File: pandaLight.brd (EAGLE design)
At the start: 100 x 50 mm, 161 parts, among them J1 PJ-037A, U1 MIC23450AAAYML, U10 AS4C128M16D3, U11 PMOD-2X6, U12 PMOD-2X6, U13 PLR135-T10, U14 PLT133-T10W, U15 PLR135-T10, U16 TP10SQ, U17 TP10SQ, U18 PAN1322, U2 6SLX45CSG324, U3 TPD4S014SON, U4 FT2232HL, U5 93LC46BT-I/OT, U6 TPD12S016PWR, U7 TPD12S016PWR, U8 N25Q128AF8, U9 TPD12S016PWR, X1 USBUB-S, X2 HDMI_RECEPTICAL_A, X3 HDMI_RECEPTICAL_A, X4 HDMI_RECEPTICAL_A, Y1 403, Y2 20Mhz

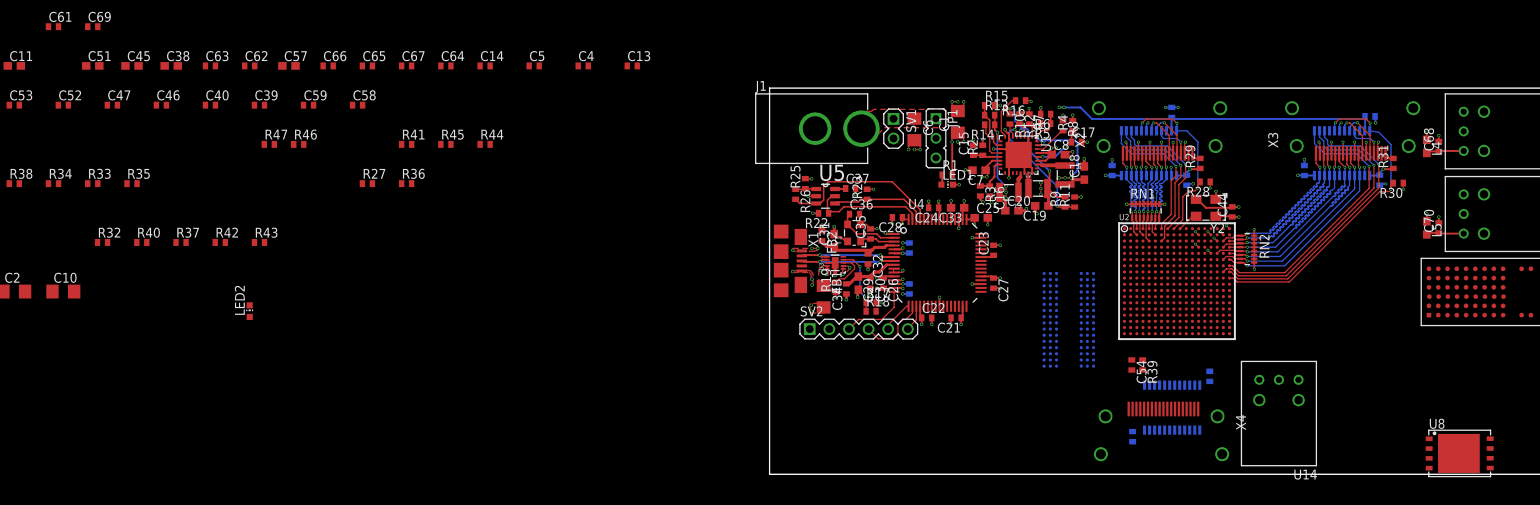
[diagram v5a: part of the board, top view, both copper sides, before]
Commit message: Placed some bypass capacitors
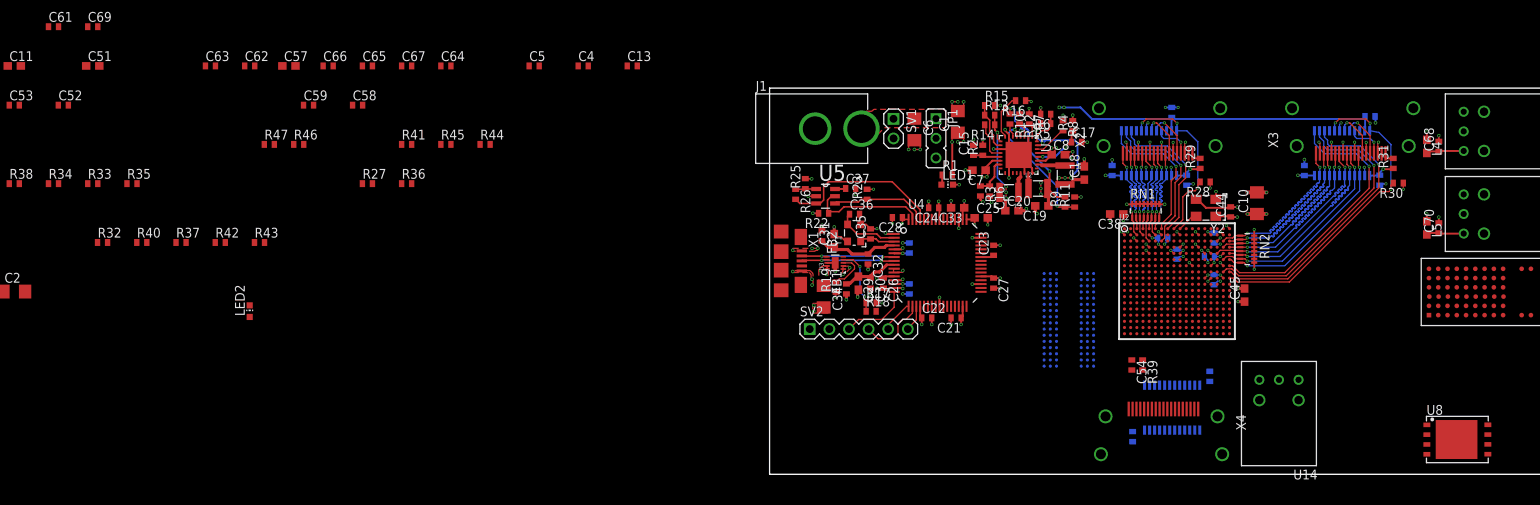
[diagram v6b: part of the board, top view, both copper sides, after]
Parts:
- moved C10 155.0 mm to (63.1, 35.1), turned to 90 degrees
- moved C45 147.1 mm to (61.5, 23.2), turned to 90 degrees
- moved C47 144.4 mm to (57.5, 25.2), flipped to the bottom, turned to 270 degrees
- moved C46 137.1 mm to (57.0, 28.2), flipped to the bottom
- moved C40 131.1 mm to (57.5, 30.6), flipped to the bottom, turned to 270 degrees
- moved C38 123.9 mm to (45.0, 33.7), turned to 180 degrees
- moved C39 118.2 mm to (50.9, 30.6), flipped to the bottom, turned to 180 degrees
- moved C14 92.8 mm to (52.8, 28.5), flipped to the bottom, turned to 270 degrees
- moved U8 1.82 mm to (89.0, 4.50)
- moved C44 0.20 mm to (59.7, 34.0)
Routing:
- net +3V3: track 58.0 -> 77.0 mm, vias 31 -> 47
- net GND: track 104.1 -> 116.9 mm, vias 90 -> 107
- net N$28: track 11.0 -> 10.1 mm
- net N$7: track 13.4 -> 12.8 mm

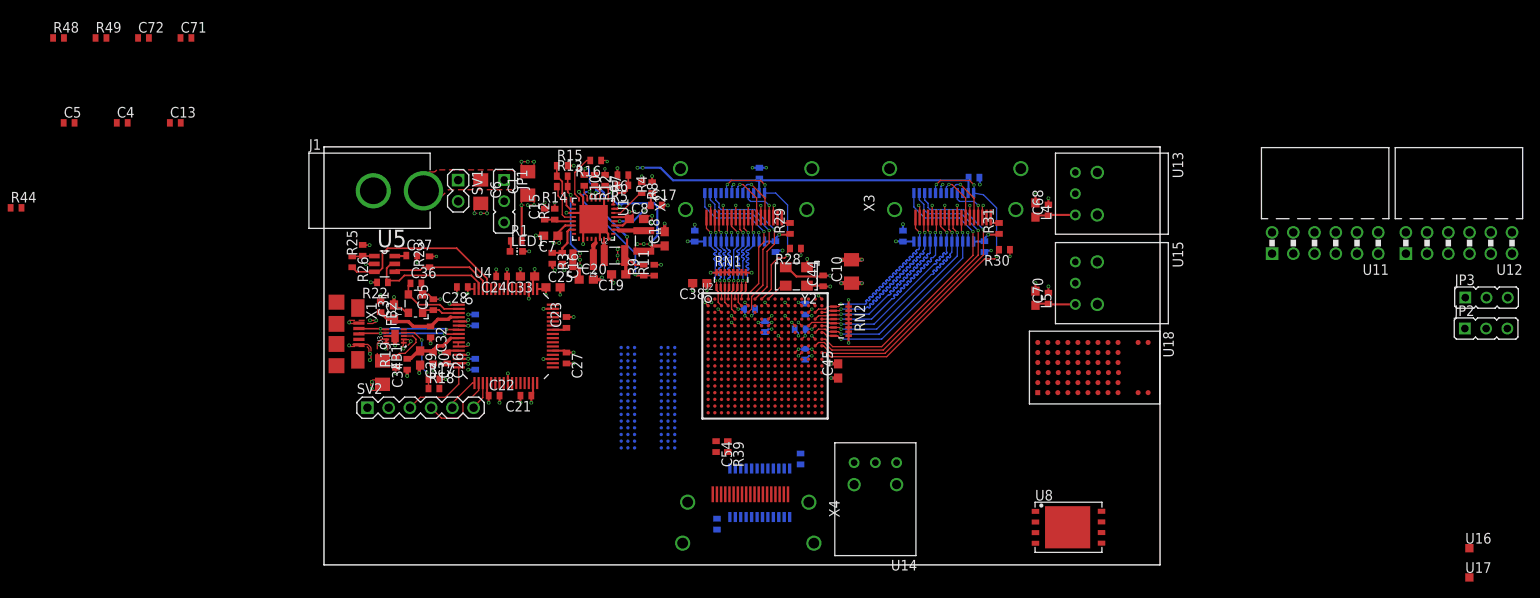
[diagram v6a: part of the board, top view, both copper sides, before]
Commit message: Routed blutooth module
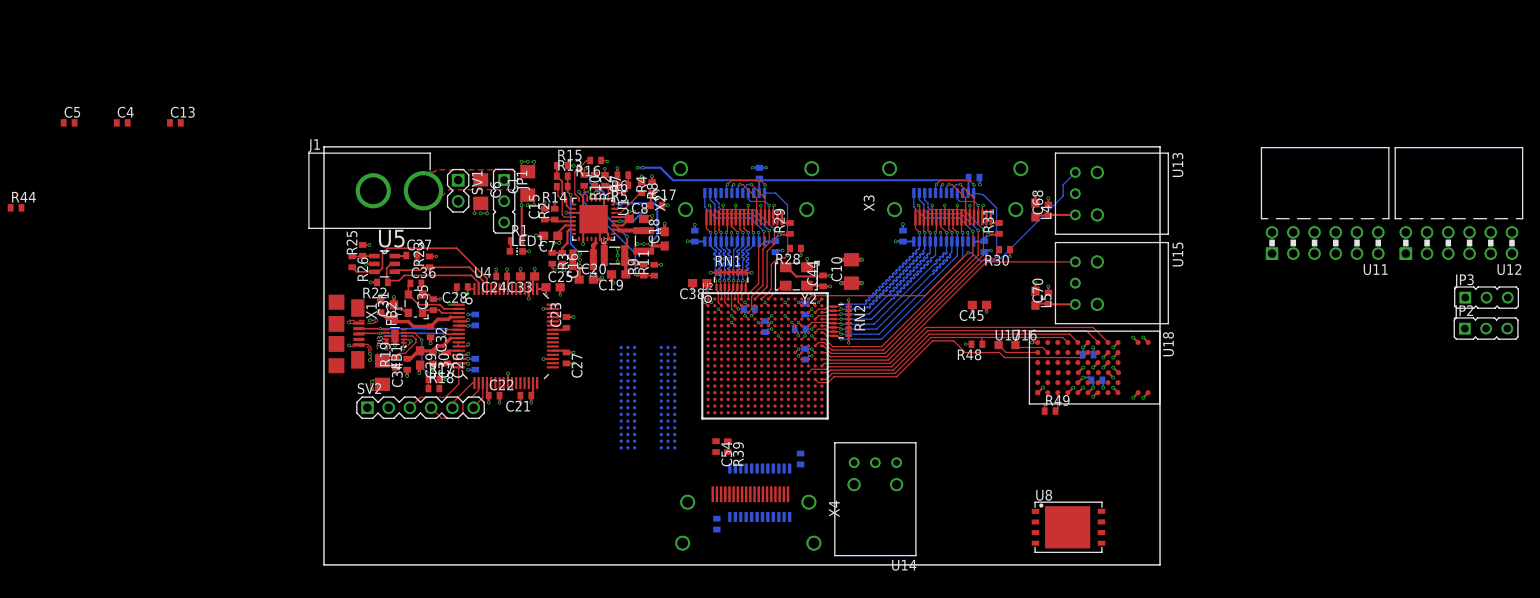
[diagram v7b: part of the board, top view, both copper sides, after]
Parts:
- moved R49 122.0 mm to (86.8, 18.4)
- moved C72 119.2 mm to (91.4, 25.1), flipped to the bottom, turned to 180 degrees
- moved C71 116.4 mm to (92.5, 22.1), flipped to the bottom, turned to 180 degrees
- moved R48 115.8 mm to (78.1, 26.4), turned to 180 degrees
- moved U17 62.8 mm to (80.7, 26.3)
- moved U16 59.5 mm to (82.7, 26.3)
- moved C45 18.7 mm to (78.4, 31.1), turned to 180 degrees
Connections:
- net BT_CTS: now also U2.M18; no longer U2.V4
- net BT_RESET#: now also U2.P17; no longer U2.V5
- net BT_RTS: now also U2.L18; no longer U2.T4
- net BT_RX: now also U2.N17; no longer U2.T3
- net BT_TX: now also U2.M16; no longer U2.R3
- net BT_WAKE: now also U2.N18; no longer U2.U5
- net TOS_IN0: now also U2.A16
- net TOS_IN1: now also U2.K18
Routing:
- net TOS_IN0: track 0.00 -> 39.8 mm, vias 0 -> 1
- net BT_TX: track 0.00 -> 37.3 mm
- net BT_RTS: track 0.00 -> 36.9 mm
- net BT_RX: track 0.00 -> 35.9 mm
- net TOS_IN1: track 0.00 -> 35.2 mm
- net BT_CTS: track 0.00 -> 33.0 mm
- net BT_WAKE: track 0.00 -> 32.6 mm
- net GND: track 116.9 -> 131.9 mm, vias 107 -> 125
- net +3V3: track 77.0 -> 85.8 mm, vias 47 -> 54
- net N$19: track 0.00 -> 5.05 mm
- net N$29: track 0.00 -> 4.25 mm
- net BT_RESET#: track 0.00 -> 2.32 mm
